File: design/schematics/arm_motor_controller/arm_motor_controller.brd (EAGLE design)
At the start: 97.2 x 54.6 mm, 65 parts, among them Q1 PFET-FQP27P06, Q2 PFET-FQP27P06, Q3 NFET-FQP30N06L, Q4 NFET-FQP30N06L, Q5 PFET-FQP27P06, Q6 PFET-FQP27P06, Q7 NFET-FQP30N06L, Q8 NFET-FQP30N06L

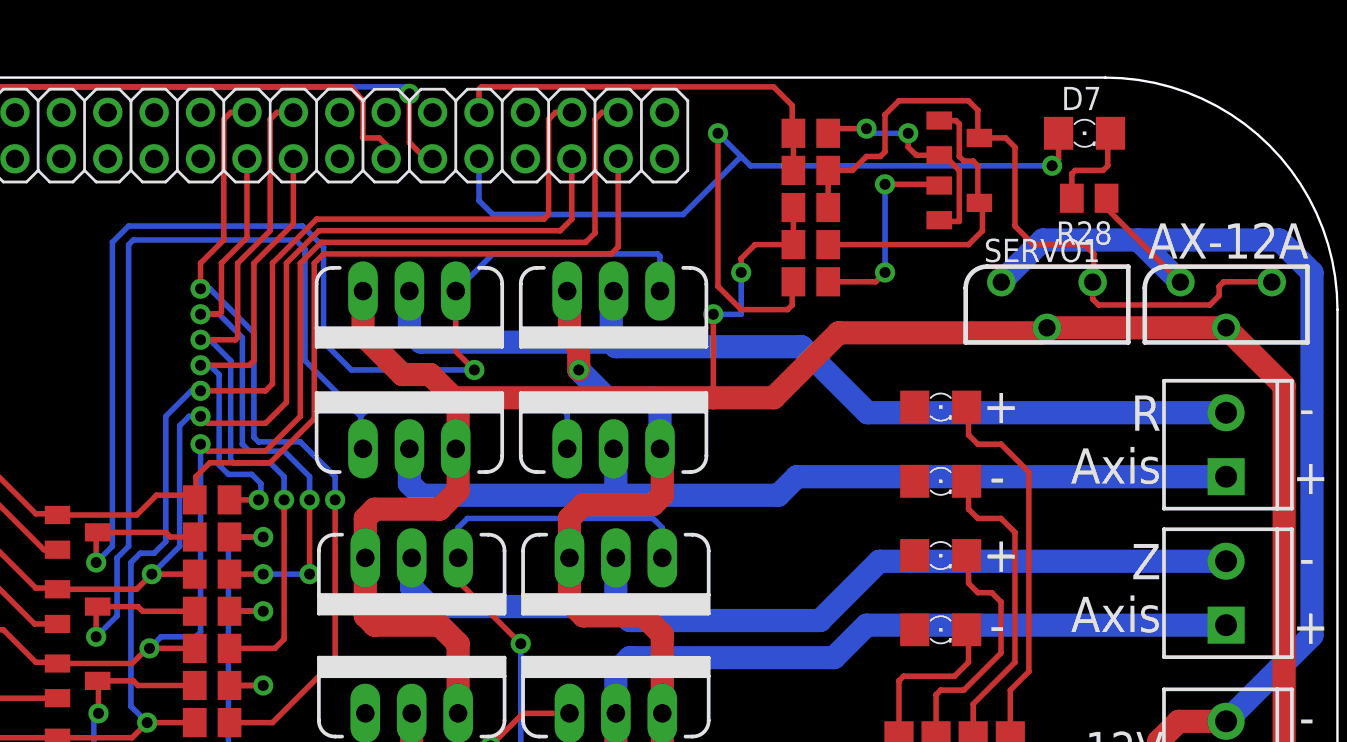
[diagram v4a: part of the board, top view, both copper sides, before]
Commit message: updated routes.
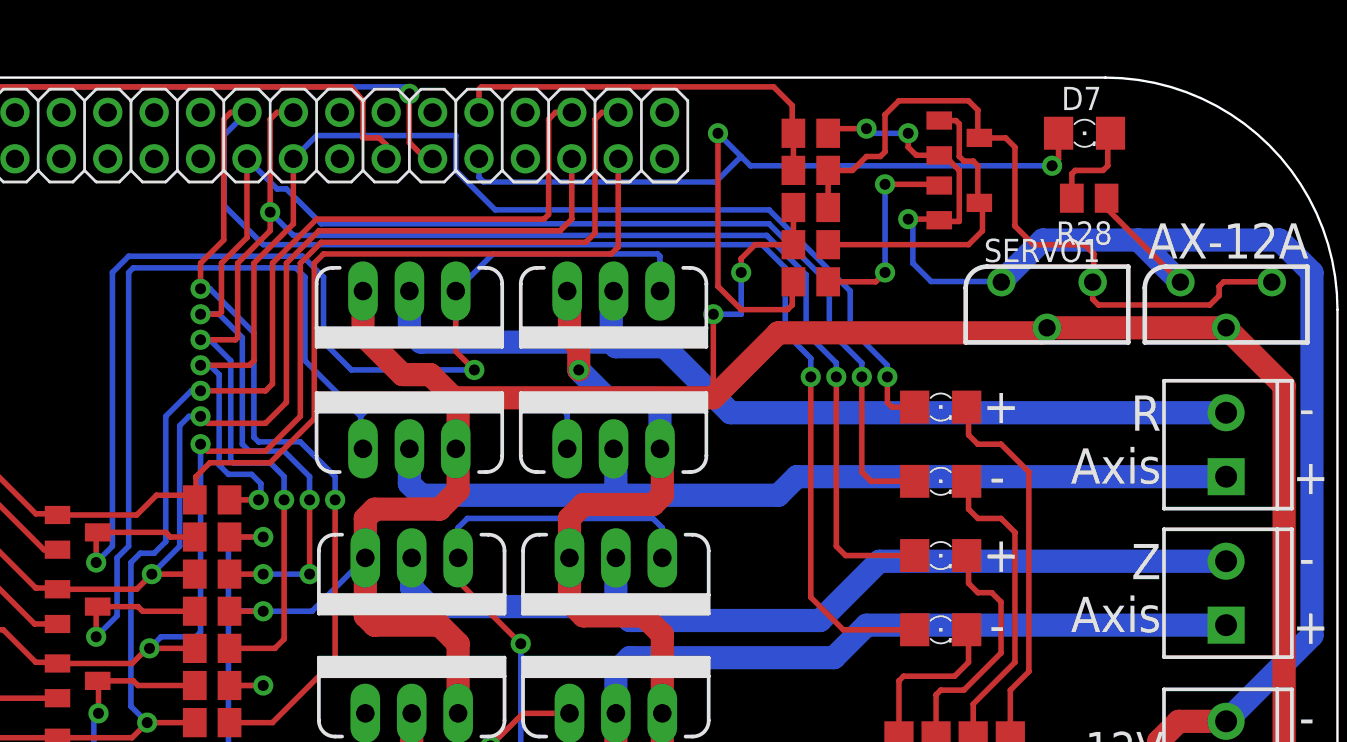
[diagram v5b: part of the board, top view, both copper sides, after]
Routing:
- net -HEIGHT: track 43.4 -> 106.2 mm, vias 2 -> 3
- net +HEIGHT: track 39.1 -> 90.0 mm, vias 2 -> 4
- net -RADIUS: track 32.9 -> 81.8 mm, vias 4 -> 5
- net +RADIUS: track 26.4 -> 70.6 mm, vias 2 -> 3
- net GND: track 372.8 -> 382.3 mm, vias 3 -> 4
- net 12V: track 156.2 -> 163.0 mm
- net N$14: track 70.4 -> 67.1 mm
- net N$13: track 65.3 -> 62.2 mm
- net BBB_TX: track 53.6 -> 51.4 mm

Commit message: finalizing motor control board.
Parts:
- moved VERTICAL_ENCODER 11.0 mm to (13.7, 16.6)
- moved RADIAL_ENCODER 10.9 mm to (13.7, 27.9)
- moved D2 4.38 mm to (17.7, 11.2), turned to 90 degrees
- moved C3 1.02 mm to (13.1, 9.14)
- renumbered Q1 to PFET01, Q2 to PFET02, Q3 to NFET01, Q4 to NFET02, Q5 to PFET03, Q6 to PFET04, Q7 to NFET03, Q8 to NFET04
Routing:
- net 5V: track 53.8 -> 38.1 mm
- net VERTICAL_ENCODER_B: track 2.99 -> 16.5 mm
- net GND: track 382.3 -> 395.2 mm
- net RADIAL_ENCODER_A: track 21.5 -> 10.2 mm
- net RADIAL_ENCODER_B: track 15.4 -> 4.32 mm
- net VERTICAL_ENCODER_A: track 9.95 -> 20.0 mm
- net BBB_TX: track 51.4 -> 46.5 mm
- net VOUT: track 48.7 -> 50.3 mm
- net 12V: track 163.0 -> 162.1 mm
- net Z-: track 51.0 -> 50.3 mm
- added copper zone on layer 1, net GND
- added copper zone on layer 16, net GND
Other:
- board text added: "+ R -"
- board text added: "+ Z -"
- board text added: "AGSE Motor Controller Rev B : 2016-03-12"
- board text added: "Vanderbilt University Aerospace Design Lab"
- board text removed: "AGSE BBB Cape Rev A : 2015-02-26"
- board text removed: "Vanderbilt University Aerospace Club"

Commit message: finalizing motor controller.
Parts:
- moved R17 7.52 mm to (18.4, 46.7), turned to 180 degrees
- moved R21 6.87 mm to (18.4, 40.6), turned to 180 degrees
- moved R20 6.08 mm to (18.4, 44.7), turned to 180 degrees
- moved R24 5.82 mm to (18.4, 42.7), turned to 180 degrees
- moved R22 4.74 mm to (11.8, 40.6), turned to 0 degrees
- moved R18 4.74 mm to (11.8, 46.7), turned to 0 degrees
- moved R26 4.72 mm to (79.5, 15.2), turned to 0 degrees
- moved R3 4.02 mm to (79.5, 21.3), turned to 0 degrees
- moved R23 2.44 mm to (11.8, 42.7), turned to 0 degrees
- moved R19 2.44 mm to (11.8, 44.7), turned to 0 degrees
- moved R27 1.93 mm to (79.5, 17.3), turned to 0 degrees
- moved R25 1.30 mm to (79.5, 19.3), turned to 0 degrees
- moved D2 0.25 mm to (17.7, 10.9)
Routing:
- net RADIAL_ENCODER_A: track 10.2 -> 23.1 mm
- net RADIAL_ENCODER_B: track 4.32 -> 16.9 mm
- net VERTICAL_ENCODER_B: track 16.5 -> 28.0 mm
- net VERTICAL_ENCODER_A: track 20.0 -> 29.0 mm
- net N$2: track 20.4 -> 26.1 mm
- net N$5: track 8.91 -> 3.58 mm
- net GND: track 395.2 -> 398.9 mm
- net N$1: track 16.6 -> 19.3 mm
- net BBB_EQEP1A: track 59.7 -> 62.5 mm
- net BBB_EQEP2A: track 18.7 -> 16.8 mm
- net BBB_EQEP2B: track 15.6 -> 16.9 mm
- net N$6: track 13.2 -> 12.3 mm

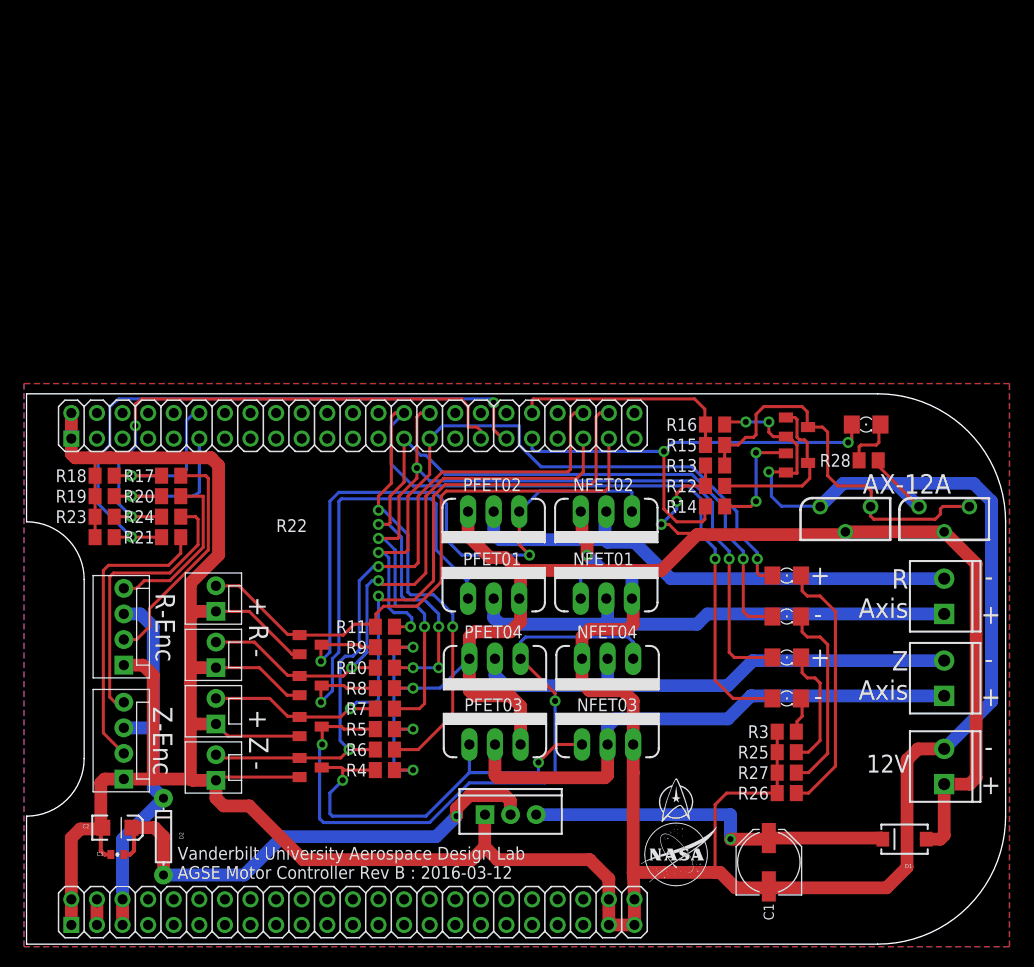
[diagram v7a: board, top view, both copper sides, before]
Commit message: updated boards and BoM.  added PTCs, changed to molex connectors, and updated diode and other componenets.
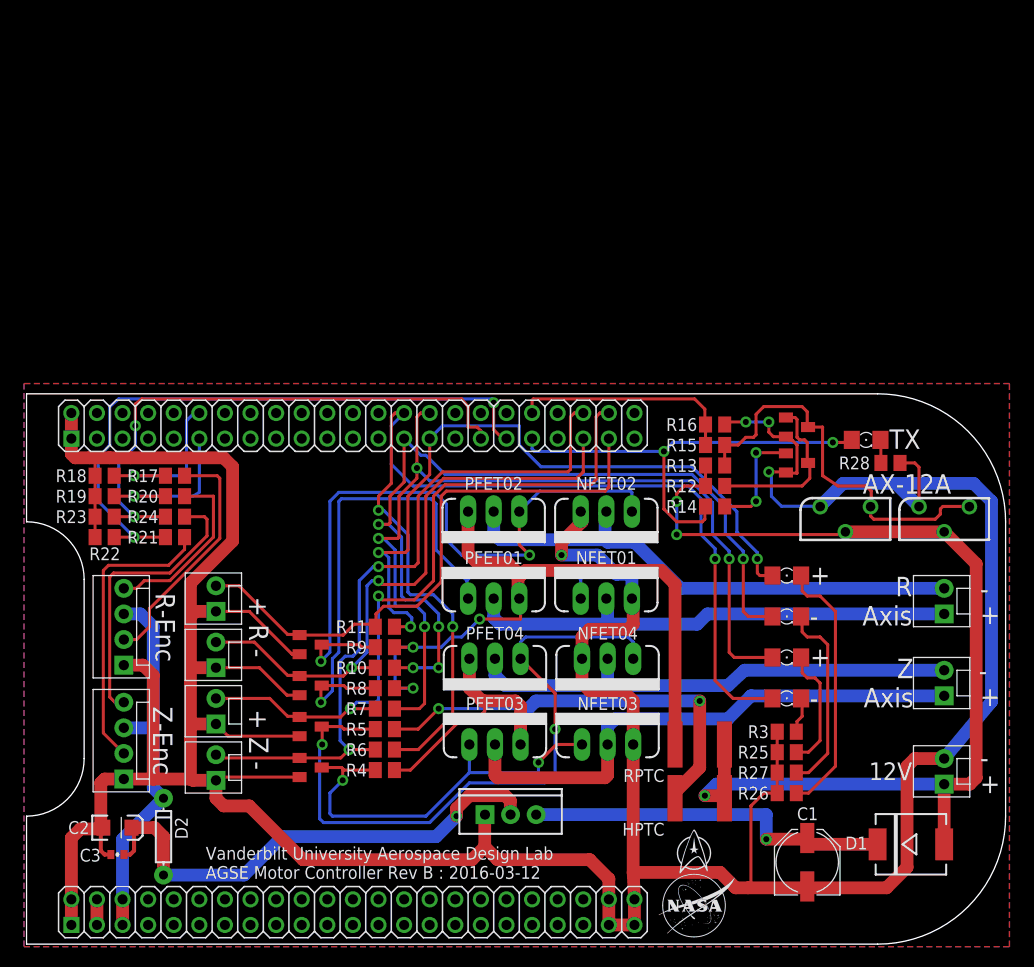
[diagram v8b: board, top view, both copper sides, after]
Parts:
- added HPTC, RPTC: MF-SMDF050, fuse:MF-SMDF050
- D1: value (none) -> 3A/600V; device SparkFun-DiscreteSemi:SMA-DIODE -> SparkFun-DiscreteSemi:SMC
- JP1, R-AXIS, Z-AXIS: value M023.5MM -> M02POLAR; device SparkFun-Connectors:SCREWTERMINAL-3.5MM-2 -> SparkFun-Connectors:MOLEX-1X2
- moved C1 3.81 mm to (81.5, 8.38)
- moved R28 2.17 mm to (89.8, 48.0)
- moved D7 1.52 mm to (87.4, 50.3)
- moved D1 0.81 mm to (91.8, 10.2), turned to 0 degrees
- moved R17 0.38 mm to (18.8, 46.7)
- moved R20 0.38 mm to (18.8, 44.7)
- moved R21 0.38 mm to (18.8, 40.6)
- moved R24 0.38 mm to (18.8, 42.7)
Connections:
- removed net 12V: D1.A, JP1.1, PFET01.3, PFET02.3, PFET03.3, PFET04.3, R12.2, R13.2, R4.2, R5.2, R8.2, R9.2, SERVO.P$2, SERVO1.P$2
- new net +12V: D1.A, HPTC.1, JP1.1, R12.2, R13.2, RPTC.1, SERVO.P$2, SERVO1.P$2
- new net H_VDD: HPTC.2, PFET03.3, PFET04.3, R4.2, R5.2
- new net R_VDD: PFET01.3, PFET02.3, R8.2, R9.2, RPTC.2
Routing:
- net 12V: track 162.1 -> 0.00 mm, vias 6 -> 0
- net +12V: track 0.00 -> 102.6 mm, vias 0 -> 3
- net H_VDD: track 0.00 -> 70.9 mm, vias 0 -> 2
- net R_VDD: track 0.00 -> 69.7 mm, vias 0 -> 3
- net N$9: track 5.33 -> 2.30 mm
- net GND: track 398.9 -> 401.5 mm
- net BBB_TX: track 46.5 -> 45.1 mm
- net RADIAL_ENCODER_A: track 23.1 -> 24.3 mm
- net RADIAL_ENCODER_B: track 16.9 -> 17.9 mm
- net VERTICAL_ENCODER_B: track 28.0 -> 28.9 mm
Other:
- board text added: "TX"
